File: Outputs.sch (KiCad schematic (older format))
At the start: 19 parts, among them P10 CONN_6, P11 CONN_8, P13 CONN_6, P8 CONN_8, P9 CONN_8

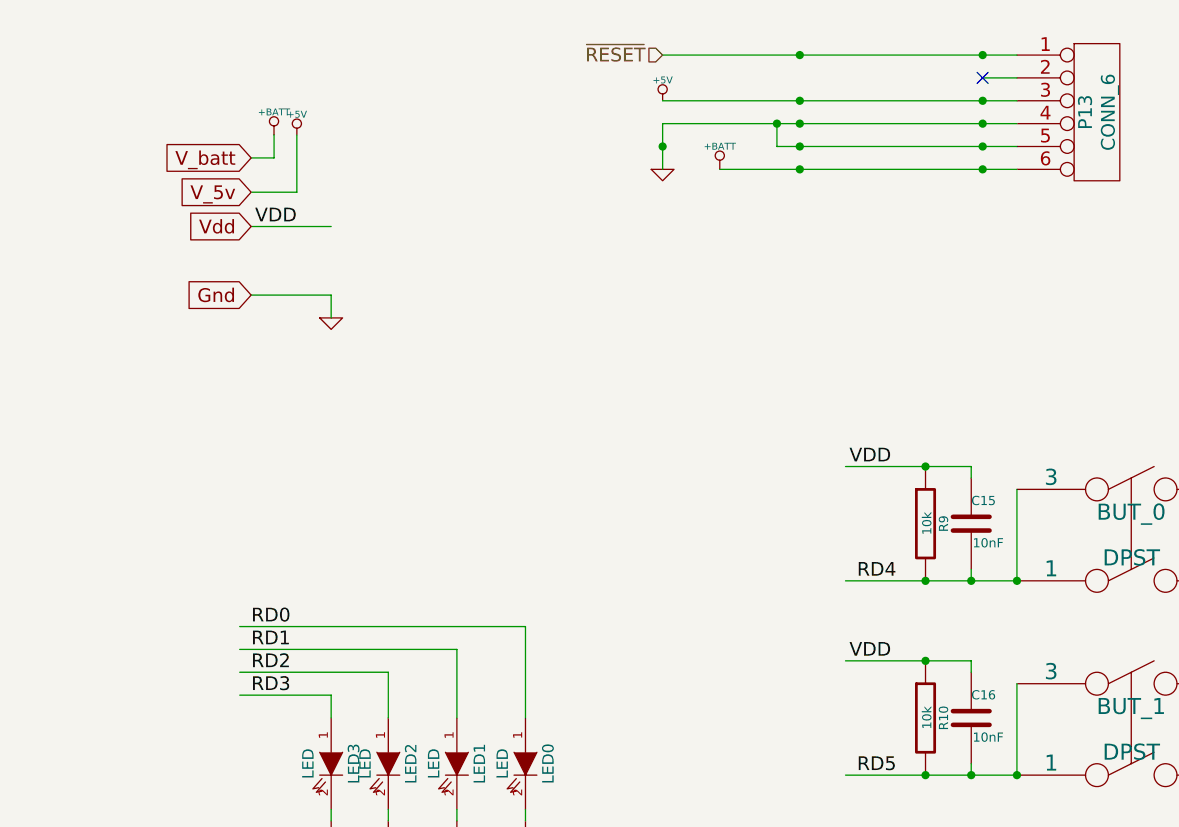
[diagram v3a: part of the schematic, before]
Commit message: Changed the board to use 3.3v rather than 5v. Total new layout.
Since the FTDI chip cannot communicate with the 5v PIC. So run
the PIC at 3.3v This limits the maximum crystal frequency of
the pic, but 4MHz is fine. the internal usb regulator is no
longer used and is replaced with the external one.

The 3.3v regulator get it's 5v from the selected 5v source.
5v is still used by the FTDI chip and the Motor driver.

Signed-off-by: Kolijn Wolfaardt <kolijn.wolfaardt@gmail.com>
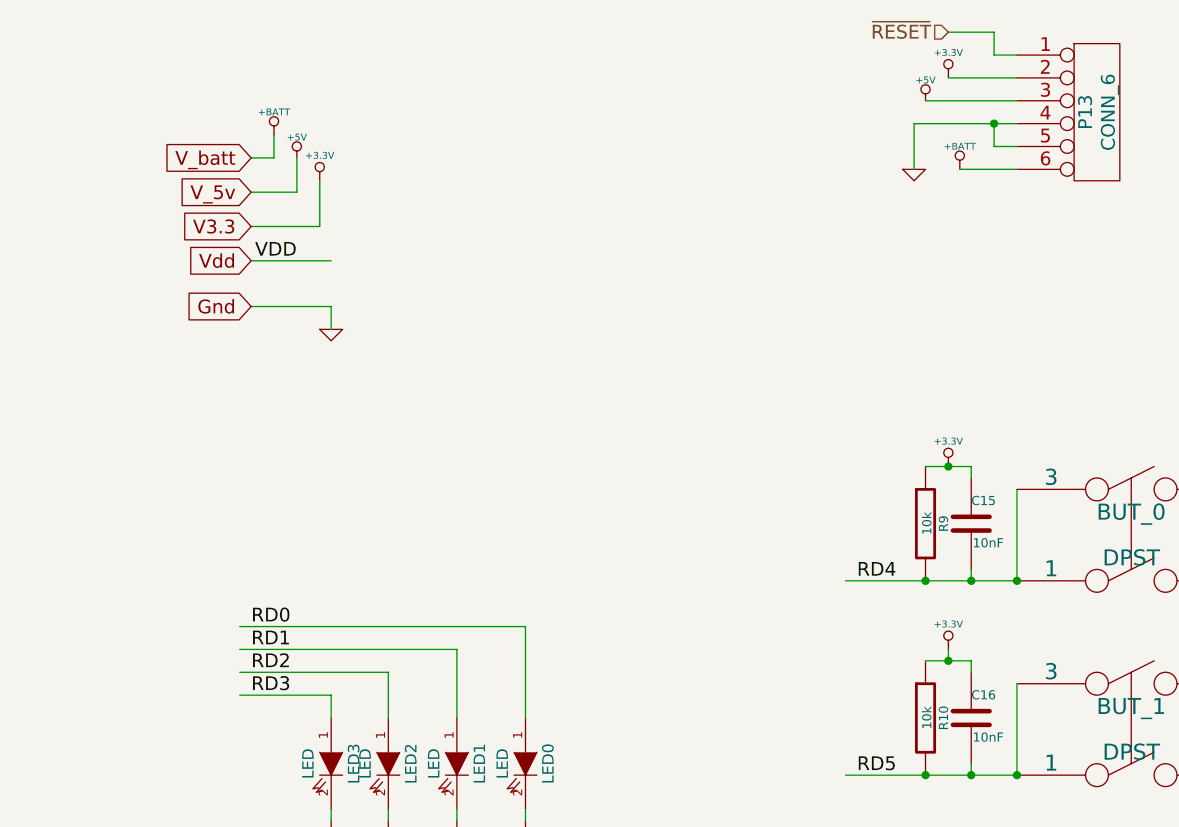
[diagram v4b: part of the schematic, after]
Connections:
- net labels added: +3.3V, V3.3
- wire segments 78 -> 83
- no-connect marks 1 -> 0
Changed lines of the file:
@@
 LIBS:l293
 LIBS:FT230x
+LIBS:33vReg
 LIBS:Robotics Board-cache
 EELAYER 27 0
@@
 Sheet 5 6
 Title ""
-Date "19 apr 2014"
+Date "20 apr 2014"
 Rev ""
 Comp ""
@@
 $EndComp
 $Comp
-L GND #PWR045
+L GND #PWR048
 U 1 1 52F7FC4E
 P 5500 5000
-F 0 "#PWR045" H 5500 5000 30  0001 C CNN
+F 0 "#PWR048" H 5500 5000 30  0001 C CNN
 F 1 "GND" H 5500 4930 30  0001 C CNN
 F 2 "" H 5500 5000 60  0000 C CNN
@@
 	1    0    0    -1
 $EndComp
-Text Label 7700 2750 2    60   ~ 0
-VDD
-$Comp
-L GND #PWR046
+$Comp
+L GND #PWR049
 U 1 1 52F7FE89
 P 9300 3400
-F 0 "#PWR046" H 9300 3400 30  0001 C CNN
+F 0 "#PWR049" H 9300 3400 30  0001 C CNN
 F 1 "GND" H 9300 3330 30  0001 C CNN
 F 2 "" H 9300 3400 60  0000 C CNN
@@
 $EndComp
 $Comp
-L R R10
-U 1 1 52F7FEA6
-P 7850 3850
-F 0 "R10" V 7930 3850 40  0000 C CNN
-F 1 "10k" V 7857 3851 40  0000 C CNN
-F 2 "~" V 7780 3850 30  0000 C CNN
-F 3 "~" H 7850 3850 30  0000 C CNN
-	1    7850 3850
-	1    0    0    -1
-$EndComp
-Text Label 7700 3600 2    60   ~ 0
-VDD
-$Comp
-L GND #PWR047
+L GND #PWR050
 U 1 1 52F7FEB7
 P 9300 4250
-F 0 "#PWR047" H 9300 4250 30  0001 C CNN
+F 0 "#PWR050" H 9300 4250 30  0001 C CNN
 F 1 "GND" H 9300 4180 30  0001 C CNN
 F 2 "" H 9300 4250 60  0000 C CNN
@@
 $EndComp
 $Comp
-L GND #PWR048
+L GND #PWR051
 U 1 1 52F799A9
-P 6700 1450
-F 0 "#PWR048" H 6700 1450 30  0001 C CNN
-F 1 "GND" H 6700 1380 30  0001 C CNN
-F 2 "" H 6700 1450 60  0000 C CNN
-F 3 "" H 6700 1450 60  0000 C CNN
-	1    6700 1450
-	1    0    0    -1
-$EndComp
-Text GLabel 4900 2000 0    60   Input ~ 0
+P 7800 1450
+F 0 "#PWR051" H 7800 1450 30  0001 C CNN
+F 1 "GND" H 7800 1380 30  0001 C CNN
+F 2 "" H 7800 1450 60  0000 C CNN
+F 3 "" H 7800 1450 60  0000 C CNN
+	1    7800 1450
+	1    0    0    -1
+$EndComp
+Text GLabel 4900 2050 0    60   Input ~ 0
 Gnd
 Text GLabel 4900 1550 0    60   Input ~ 0
 V_5v
 $Comp
-L GND #PWR049
+L GND #PWR052
 U 1 1 52F79CA3
-P 5250 2100
-F 0 "#PWR049" H 5250 2100 30  0001 C CNN
-F 1 "GND" H 5250 2030 30  0001 C CNN
-F 2 "" H 5250 2100 60  0000 C CNN
-F 3 "" H 5250 2100 60  0000 C CNN
-	1    5250 2100
-	1    0    0    -1
-$EndComp
-Text Label 5100 1700 2    60   ~ 0
+P 5250 2150
+F 0 "#PWR052" H 5250 2150 30  0001 C CNN
+F 1 "GND" H 5250 2080 30  0001 C CNN
+F 2 "" H 5250 2150 60  0000 C CNN
+F 3 "" H 5250 2150 60  0000 C CNN
+	1    5250 2150
+	1    0    0    -1
+$EndComp
+Text Label 5100 1850 2    60   ~ 0
 VDD
 Text GLabel 4900 1400 0    60   Input ~ 0
 V_batt
 $Comp
-L +BATT #PWR050
+L +BATT #PWR053
 U 1 1 52F79EEA
 P 5000 1300
-F 0 "#PWR050" H 5000 1250 20  0001 C CNN
+F 0 "#PWR053" H 5000 1250 20  0001 C CNN
 F 1 "+BATT" H 5000 1400 30  0000 C CNN
 F 2 "" H 5000 1300 60  0000 C CNN
@@
 	1    0    0    -1
 $EndComp
-Text GLabel 4900 1700 0    60   Input ~ 0
+Text GLabel 4900 1850 0    60   Input ~ 0
 Vdd
 $Comp
-L +5V #PWR051
+L +5V #PWR054
 U 1 1 52F7A111
-P 5100 1300
-F 0 "#PWR051" H 5100 1390 20  0001 C CNN
-F 1 "+5V" H 5100 1390 30  0000 C CNN
-F 2 "" H 5100 1300 60  0000 C CNN
-F 3 "" H 5100 1300 60  0000 C CNN
-	1    5100 1300
-	1    0    0    -1
-$EndComp
-$Comp
-L +5V #PWR052
+P 5100 1400
+F 0 "#PWR054" H 5100 1490 20  0001 C CNN
+F 1 "+5V" H 5100 1490 30  0000 C CNN
+F 2 "" H 5100 1400 60  0000 C CNN
+F 3 "" H 5100 1400 60  0000 C CNN
+	1    5100 1400
+	1    0    0    -1
+$EndComp
+$Comp
+L +5V #PWR055
 U 1 1 52F7A162
-P 6700 1150
-F 0 "#PWR052" H 6700 1240 20  0001 C CNN
-F 1 "+5V" H 6700 1240 30  0000 C CNN
-F 2 "" H 6700 1150 60  0000 C CNN
-F 3 "" H 6700 1150 60  0000 C CNN
-	1    6700 1150
-	1    0    0    -1
-$EndComp
-$Comp
-L +BATT #PWR053
+P 7850 1150
+F 0 "#PWR055" H 7850 1240 20  0001 C CNN
+F 1 "+5V" H 7850 1240 30  0000 C CNN
+F 2 "" H 7850 1150 60  0000 C CNN
+F 3 "" H 7850 1150 60  0000 C CNN
+	1    7850 1150
+	1    0    0    -1
+$EndComp
+$Comp
+L +BATT #PWR056
 U 1 1 52F7A168
-P 6950 1450
-F 0 "#PWR053" H 6950 1400 20  0001 C CNN
-F 1 "+BATT" H 6950 1550 30  0000 C CNN
-F 2 "" H 6950 1450 60  0000 C CNN
-F 3 "" H 6950 1450 60  0000 C CNN
-	1    6950 1450
-	1    0    0    -1
-$EndComp
-Text HLabel 6700 950  0    60   Input ~ 0
+P 8000 1450
+F 0 "#PWR056" H 8000 1400 20  0001 C CNN
+F 1 "+BATT" H 8000 1550 30  0000 C CNN
+F 2 "" H 8000 1450 60  0000 C CNN
+F 3 "" H 8000 1450 60  0000 C CNN
+	1    8000 1450
+	1    0    0    -1
+$EndComp
+Text HLabel 7950 850  0    60   Input ~ 0
 ~RESET
 Text HLabel 1950 5450 0    60   Input ~ 0
@@
 	6100 3450 6100 3850
 Wire Wire Line
-	7500 2750 8050 2750
-Wire Wire Line
 	8250 3250 8250 2850
 Connection ~ 8250 3250
 Wire Wire Line
 	9300 2850 9300 3400
-Wire Wire Line
-	7500 3600 8050 3600
 Wire Wire Line
 	8250 4100 8250 3700
@@
 Connection ~ 3100 2600
 Wire Wire Line
-	6700 950  8250 950
-Connection ~ 8100 950
-Wire Wire Line
-	6700 1150 8250 1150
-Connection ~ 8100 1150
-Wire Wire Line
-	6700 1250 8250 1250
-Connection ~ 8100 1250
-Wire Wire Line
-	7200 1350 8250 1350
-Connection ~ 8100 1350
-Wire Wire Line
-	6950 1450 8250 1450
-Connection ~ 8100 1450
-Connection ~ 7300 950
-Connection ~ 7300 1150
-Wire Wire Line
-	6700 1250 6700 1450
-Connection ~ 7300 1250
-Connection ~ 7300 1350
-Connection ~ 6700 1350
-Wire Wire Line
-	5250 2000 5250 2100
-Wire Wire Line
-	4900 2000 5250 2000
-Wire Wire Line
-	4900 1700 5250 1700
+	7800 1250 7800 1450
+Wire Wire Line
+	5250 2050 5250 2150
+Wire Wire Line
+	4900 2050 5250 2050
+Wire Wire Line
+	4900 1850 5250 1850
 Wire Wire Line
 	4900 1400 5000 1400
@@
 	4900 1550 5100 1550
 Wire Wire Line
-	5100 1550 5100 1300
-Wire Wire Line
-	7200 1350 7200 1250
-Connection ~ 7200 1250
-Connection ~ 7300 1450
+	5100 1550 5100 1400
 Wire Wire Line
 	1950 5450 3200 5450
@@
 Wire Wire Line
 	8050 3600 8050 3650
-Connection ~ 7850 3600
 Wire Wire Line
 	8050 4050 8050 4100
@@
 Wire Wire Line
 	8050 2750 8050 2800
-Connection ~ 7850 2750
 Wire Wire Line
 	8050 3200 8050 3250
@@
 	9250 3250 9300 3250
 Connection ~ 9300 3250
-NoConn ~ 8100 1050
-Wire Wire Line
-	8100 1050 8250 1050
+Wire Wire Line
+	7950 1050 8250 1050
+Text GLabel 4900 1700 0    60   Input ~ 0
+V3.3
+$Comp
+L +3.3V #PWR057
+U 1 1 53538049
+P 5200 1500
+F 0 "#PWR057" H 5200 1460 30  0001 C CNN
+F 1 "+3.3V" H 5200 1610 30  0000 C CNN
+F 2 "" H 5200 1500 60  0000 C CNN
+F 3 "" H 5200 1500 60  0000 C CNN
+	1    5200 1500
+	1    0    0    -1
+$EndComp
+Wire Wire Line
+	4900 1700 5200 1700
+Wire Wire Line
+	5200 1700 5200 1500
+$Comp
+L +3.3V #PWR058
+U 1 1 53538103
+P 7950 1050
+F 0 "#PWR058" H 7950 1010 30  0001 C CNN
+F 1 "+3.3V" H 7950 1160 30  0000 C CNN
+F 2 "" H 7950 1050 60  0000 C CNN
+F 3 "" H 7950 1050 60  0000 C CNN
+	1    7950 1050
+	1    0    0    -1
+$EndComp
+Wire Wire Line
+	8250 1150 7850 1150
+Wire Wire Line
+	7950 850  8150 850
+Wire Wire Line
+	8150 850  8150 950
+Wire Wire Line
+	8150 950  8250 950
+Wire Wire Line
+	8000 1450 8250 1450
+Wire Wire Line
+	8250 1350 8150 1350
+Wire Wire Line
+	8150 1350 8150 1250
+Wire Wire Line
+	7800 1250 8250 1250
+Connection ~ 8150 1250
+$Comp
+L +3.3V #PWR059
+U 1 1 535384DE
+P 7950 2750
+F 0 "#PWR059" H 7950 2710 30  0001 C CNN
+F 1 "+3.3V" H 7950 2860 30  0000 C CNN
+F 2 "" H 7950 2750 60  0000 C CNN
+F 3 "" H 7950 2750 60  0000 C CNN
+	1    7950 2750
+	1    0    0    -1
+$EndComp
+Wire Wire Line
+	7850 2750 8050 2750
+Connection ~ 7950 2750
+$Comp
+L R R10
+U 1 1 52F7FEA6
+P 7850 3850
+F 0 "R10" V 7930 3850 40  0000 C CNN
+F 1 "10k" V 7857 3851 40  0000 C CNN
+F 2 "~" V 7780 3850 30  0000 C CNN
+F 3 "~" H 7850 3850 30  0000 C CNN
+	1    7850 3850
+	1    0    0    -1
+$EndComp
+Wire Wire Line
+	8050 3600 7850 3600
+$Comp
+L +3.3V #PWR060
+U 1 1 535386B3
+P 7950 3550
+F 0 "#PWR060" H 7950 3510 30  0001 C CNN
+F 1 "+3.3V" H 7950 3660 30  0000 C CNN
+F 2 "" H 7950 3550 60  0000 C CNN
+F 3 "" H 7950 3550 60  0000 C CNN
+	1    7950 3550
+	1    0    0    -1
+$EndComp
+Wire Wire Line
+	7950 3550 7950 3600
+Connection ~ 7950 3600
 $EndSCHEMATC
